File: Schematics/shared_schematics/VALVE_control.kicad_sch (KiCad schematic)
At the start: 7 parts, among them J2 SOL_CONN, Q1 AO3400A

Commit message: add requested changes for PR
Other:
- note added: "0.1 µF in 0603 for low parasitics and fast HF response; 10 µF in 1206 for larger bulk charge."
- note added: "package choice also affected by DC Bias Effect, higher cap MLCCs in smaller packages lose a significant pct of their effective capacitance."
- note added: "parallel decoupling circuit at the solenoid connector positive to suppress fast and slow transients and provide effective decoupling. 0.1 µF for high-frequency noise, 10 µF for bulk transient suppression."
- note added: "place caps together with flyback diode as close as possible to solenoid connector to minimize inductive voltage spikes and noise pickup"
- note added: "place the 0.1uF closer to the SOL input due to faster responsiveness (HF filter) the larger cap handles LF, therefore slightly less sensitive to placement"
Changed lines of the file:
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@@
+		)
+	)
+	(text "place the 0.1uF closer to the SOL input due to faster responsiveness (HF filter)\nthe larger cap handles LF, therefore slightly less sensitive to placement\n"
+		(exclude_from_sim no)
+		(at 86.868 81.026 0)
+		(effects
+			(font
+				(size 1.27 1.27)
+				(color 0 0 0 1)
+			)
+		)
+	)
+	(text "parallel decoupling circuit at the solenoid connector positive\nto suppress fast and slow transients and provide effective decoupling.\n\n0.1 µF for high-frequency noise, 10 µF for bulk transient suppression."
+		(exclude_from_sim no)
+		(at 88.138 116.332 0)
+		(effects
+			(font
+				(size 1.016 1.016)
+				(color 0 0 0 1)
+			)
+		)
+	)
+	(text "0.1 µF in 0603 for low parasitics and fast HF response; \n10 µF in 1206 for larger bulk charge."
+		(exclude_from_sim no)
+		(at 88.138 124.968 0)
+		(effects
+			(font
+				(size 1.016 1.016)
+				(color 0 0 0 1)
+			)
+		)
+	)
+	(text "place caps together with flyback diode as close as \npossible to solenoid connector to minimize inductive voltage spikes and noise pickup"
+		(exclude_from_sim no)
+		(at 87.376 74.422 0)
+		(effects
+			(font
+				(size 1.27 1.27)
+				(color 0 0 0 1)
+			)
+		)
+	)
+	(text "package choice also affected by DC Bias Effect, higher cap MLCCs \nin smaller packages lose a significant pct of their effective\ncapacitance."
+		(exclude_from_sim no)
+		(at 138.938 125.73 0)
+		(effects
+			(font
+				(size 1.016 1.016)
+				(color 0 0 0 1)
+			)
 		)
 	)
@@
 		(dnp no)
 		(fields_autoplaced yes)
-		(property "Reference" "#PWR0101"
+		(property "Reference" "#PWR0123"
 			(at 88.9 106.68 0)
 			(effects
@@
 		)
 	)
+	(sheet_instances
+		(path "/"
+			(page "1")
+		)
+	)

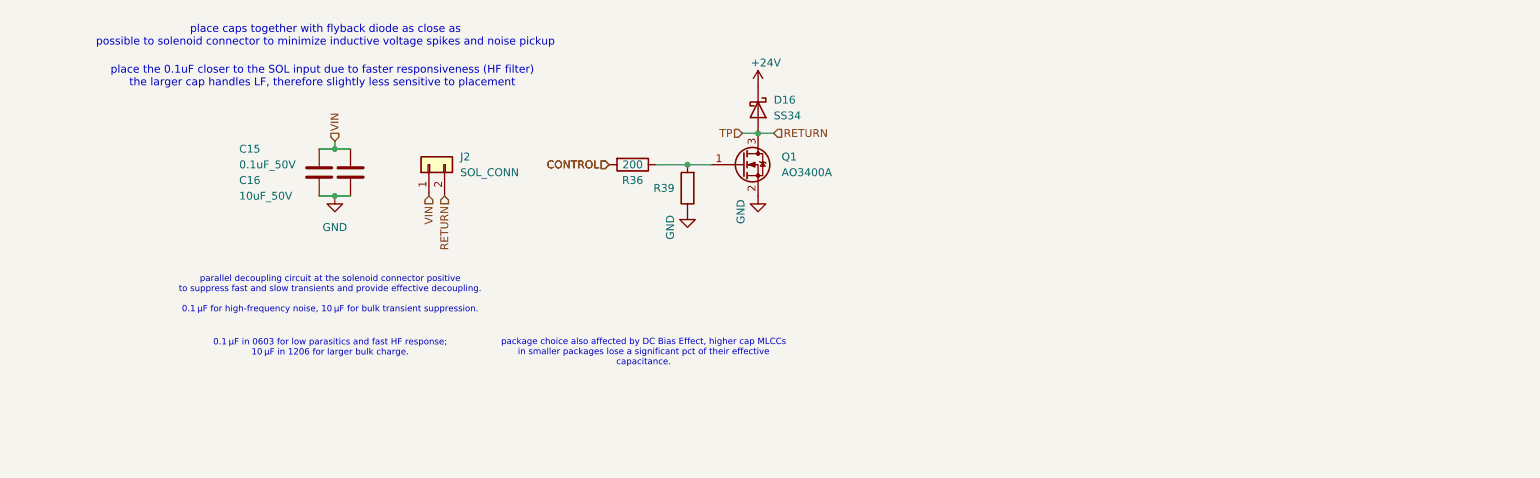
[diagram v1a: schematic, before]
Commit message: add all circuitry and missing datasheets
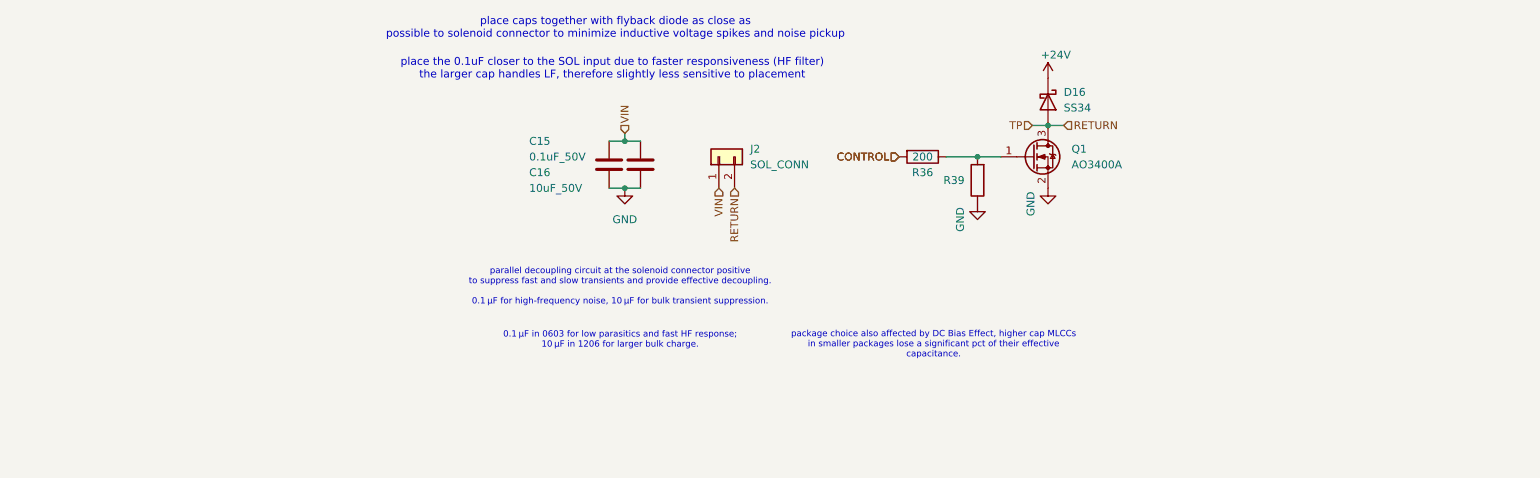
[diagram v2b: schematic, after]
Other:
- moved on the sheet: C15, C16, D16, J2, Q1, R36, R39

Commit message: pin assignments verified
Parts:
- J2: footprint CONNS:CONN02_530470260_MOL -> S02B_PASK_2:CONN2_S02B-PASK-2_JST
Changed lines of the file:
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@@
 			)
 		)
-		(property "Footprint" "CONNS:CONN02_530470260_MOL"
+		(property "Footprint" "S02B_PASK_2:CONN2_S02B-PASK-2_JST"
 			(at 151.13 93.98 0)
 			(effects

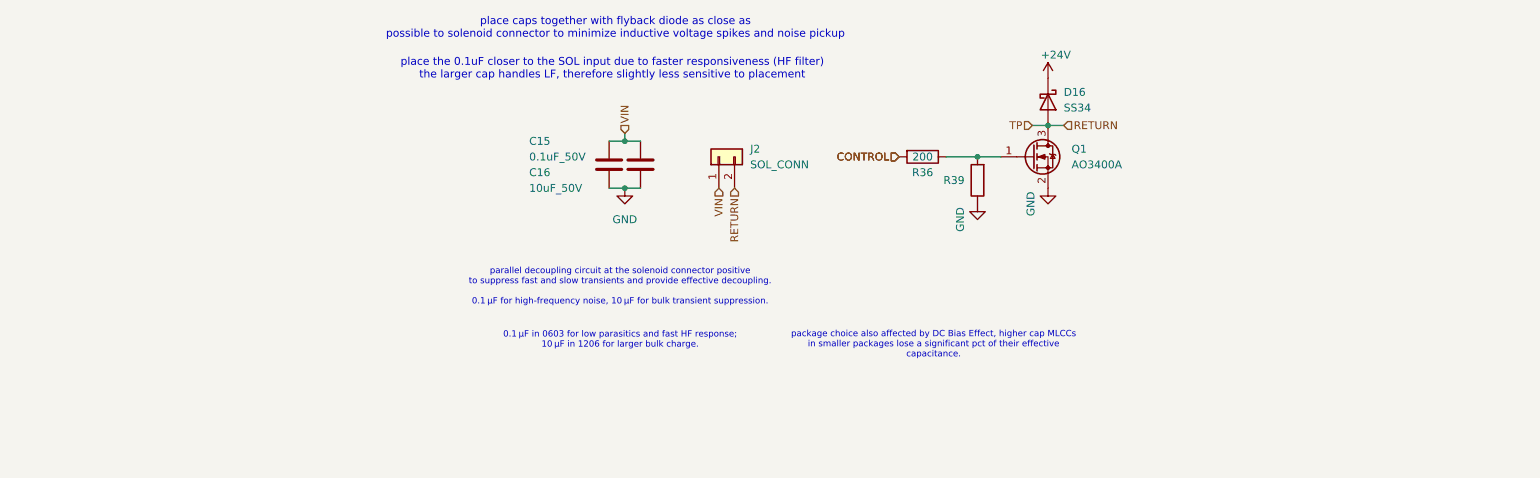
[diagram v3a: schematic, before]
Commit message: add power switching for PTs (schematic only)
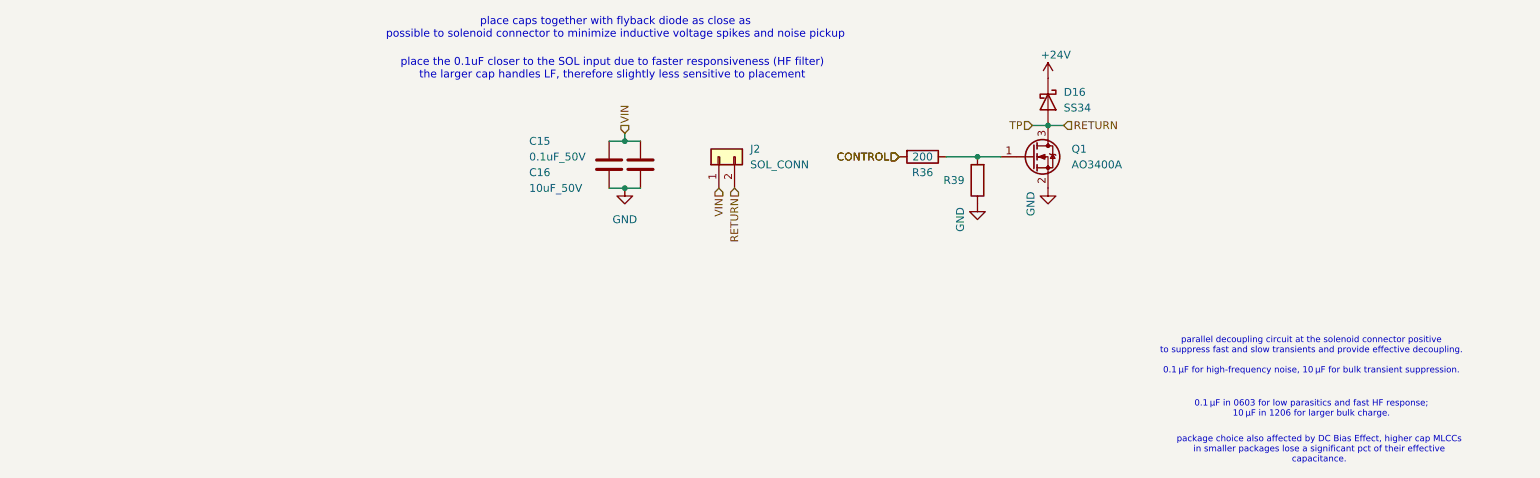
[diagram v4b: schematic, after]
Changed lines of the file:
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@@
 	(text "parallel decoupling circuit at the solenoid connector positive\nto suppress fast and slow transients and provide effective decoupling.\n\n0.1 µF for high-frequency noise, 10 µF for bulk transient suppression."
 		(exclude_from_sim no)
-		(at 135.128 115.062 0)
+		(at 247.142 126.238 0)
 		(effects
 			(font
@@
 	(text "0.1 µF in 0603 for low parasitics and fast HF response; \n10 µF in 1206 for larger bulk charge."
 		(exclude_from_sim no)
-		(at 135.128 123.698 0)
+		(at 247.142 134.874 0)
 		(effects
 			(font
@@
 	(text "package choice also affected by DC Bias Effect, higher cap MLCCs \nin smaller packages lose a significant pct of their effective\ncapacitance."
 		(exclude_from_sim no)
-		(at 185.928 124.46 0)
+		(at 248.412 141.478 0)
 		(effects
 			(font

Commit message: organizational work
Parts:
- C15: value 0.1uF_50V -> 0.1uF
- C16: value 10uF_50V -> 10uF
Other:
- note added: "place caps, FB-diode as close as possible to solenoid connectors."
- note removed: "0.1 µF in 0603 for low parasitics and fast HF response; 10 µF in 1206 for larger bulk charge."
- note removed: "package choice also affected by DC Bias Effect, higher cap MLCCs in smaller packages lose a significant pct of their effective capacitance."
- note removed: "parallel decoupling circuit at the solenoid connector positive to suppress fast and slow transients and provide effective decoupling. 0.1 µF for high-frequency noise, 10 µF for bulk transient suppression."
- note removed: "place caps together with flyback diode as close as possible to solenoid connector to minimize inductive voltage spikes and noise pickup"
- note removed: "place the 0.1uF closer to the SOL input due to faster responsiveness (HF filter) the larger cap handles LF, therefore slightly less sensitive to placement"
- moved on the sheet: C15, C16
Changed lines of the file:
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@@
 	)
 	(junction
-		(at 135.89 91.44)
+		(at 139.7 97.79)
 		(diameter 0)
 		(color 0 0 0 0)
@@
 	)
 	(junction
-		(at 135.89 99.06)
+		(at 139.7 90.17)
 		(diameter 0)
 		(color 0 0 0 0)
@@
 	(wire
 		(pts
-			(xy 135.89 90.17) (xy 135.89 91.44)
+			(xy 139.7 99.06) (xy 139.7 97.79)
 		)
 		(stroke
@@
 	(wire
 		(pts
-			(xy 135.89 91.44) (xy 138.43 91.44)
+			(xy 139.7 97.79) (xy 137.16 97.79)
 		)
 		(stroke
@@
 	(wire
 		(pts
-			(xy 133.35 99.06) (xy 135.89 99.06)
+			(xy 142.24 90.17) (xy 139.7 90.17)
 		)
 		(stroke
@@
 	(wire
 		(pts
-			(xy 133.35 91.44) (xy 135.89 91.44)
+			(xy 142.24 97.79) (xy 139.7 97.79)
 		)
 		(stroke
@@
 	(wire
 		(pts
-			(xy 135.89 99.06) (xy 138.43 99.06)
+			(xy 139.7 90.17) (xy 137.16 90.17)
 		)
 		(stroke
@@
 		)
 	)
-	(text "place the 0.1uF closer to the SOL input due to faster responsiveness (HF filter)\nthe larger cap handles LF, therefore slightly less sensitive to placement\n"
-		(exclude_from_sim no)
-		(at 133.858 79.756 0)
+	(text "place caps, FB-diode as close as possible \nto solenoid connectors."
+		(exclude_from_sim no)
+		(at 167.894 81.534 0)
 		(effects
 			(font
 				(size 1.27 1.27)
-				(color 0 0 0 1)
-			)
-		)
-	)
-	(text "parallel decoupling circuit at the solenoid connector positive\nto suppress fast and slow transients and provide effective decoupling.\n\n0.1 µF for high-frequency noise, 10 µF for bulk transient suppression."
-		(exclude_from_sim no)
-		(at 247.142 126.238 0)
-		(effects
-			(font
-				(size 1.016 1.016)
-				(color 0 0 0 1)
-			)
-		)
-	)
-	(text "0.1 µF in 0603 for low parasitics and fast HF response; \n10 µF in 1206 for larger bulk charge."
-		(exclude_from_sim no)
-		(at 247.142 134.874 0)
-		(effects
-			(font
-				(size 1.016 1.016)
-				(color 0 0 0 1)
-			)
-		)
-	)
-	(text "place caps together with flyback diode as close as \npossible to solenoid connector to minimize inductive voltage spikes and noise pickup"
-		(exclude_from_sim no)
-		(at 134.366 73.152 0)
-		(effects
-			(font
-				(size 1.27 1.27)
-				(color 0 0 0 1)
-			)
-		)
-	)
-	(text "package choice also affected by DC Bias Effect, higher cap MLCCs \nin smaller packages lose a significant pct of their effective\ncapacitance."
-		(exclude_from_sim no)
-		(at 248.412 141.478 0)
-		(effects
-			(font
-				(size 1.016 1.016)
 				(color 0 0 0 1)
 			)
@@
 	(hierarchical_label "VIN"
 		(shape input)
-		(at 135.89 90.17 90)
+		(at 139.7 99.06 270)
 		(fields_autoplaced yes)
 		(effects
@@
 				(size 1.27 1.27)
 			)
-			(justify left)
+			(justify right)
 		)
 	)
@@
 				)
 			)
-			(project "upper_lc_board"
-				(path "/d63798c4-e363-437e-9012-e4aff32e6642/762489dd-fdf2-4f5c-8c0c-d0a6195d3f58/294431a1-b811-4a1d-b2a9-ae58ba2678b8"
-					(reference "Q1")
-					(unit 1)
-				)
-				(path "/d63798c4-e363-437e-9012-e4aff32e6642/762489dd-fdf2-4f5c-8c0c-d0a6195d3f58/ba318d50-d24b-43da-9443-1d352fb2a38b"
-					(reference "Q2")
-					(unit 1)
-				)
-			)
 		)
 	)
@@
 				)
 			)
-			(project "upper_lc_board"
-				(path "/d63798c4-e363-437e-9012-e4aff32e6642/762489dd-fdf2-4f5c-8c0c-d0a6195d3f58/294431a1-b811-4a1d-b2a9-ae58ba2678b8"
-					(reference "D16")
-					(unit 1)
-				)
-				(path "/d63798c4-e363-437e-9012-e4aff32e6642/762489dd-fdf2-4f5c-8c0c-d0a6195d3f58/ba318d50-d24b-43da-9443-1d352fb2a38b"
-					(reference "D15")
-					(unit 1)
-				)
-			)
 		)
 	)
 	(symbol
 		(lib_id "power:GND")
-		(at 135.89 99.06 0)
+		(at 139.7 90.17 180)
 		(unit 1)
 		(exclude_from_sim no)
@@
 		(fields_autoplaced yes)
 		(property "Reference" "#PWR0123"
-			(at 135.89 105.41 0)
+			(at 139.7 83.82 0)
 			(effects
 				(font
@@
 		)
 		(property "Value" "GND"
-			(at 135.89 104.14 0)
+			(at 139.7 85.09 0)
 			(effects
 				(font
@@
 		)
 		(property "Footprint" ""
-			(at 135.89 99.06 0)
+			(at 139.7 90.17 0)
 			(effects
 				(font
@@
 		)
 		(property "Datasheet" ""
-			(at 135.89 99.06 0)
+			(at 139.7 90.17 0)
 			(effects
 				(font
@@
 		)
 		(property "Description" "Power symbol creates a global label with name \"GND\" , ground"
-			(at 135.89 99.06 0)
+			(at 139.7 90.17 0)
 			(effects
 				(font
@@
 	(symbol
 		(lib_id "Device:C")
-		(at 138.43 95.25 0)
+		(at 137.16 93.98 180)
 		(unit 1)
 		(exclude_from_sim no)
@@
 		(dnp no)
 		(property "Reference" "C16"
-			(at 120.396 96.52 0)
+			(at 132.08 90.17 0)
 			(effects
 				(font
@@
 			)
 		)
-		(property "Value" "10uF_50V"
-			(at 120.396 99.06 0)
+		(property "Value" "10uF"
+			(at 132.08 92.71 0)
 			(effects
 				(font
@@
 		)
 		(property "Footprint" "Capacitor_SMD:C_1206_3216Metric"
-			(at 139.3952 99.06 0)
+			(at 136.1948 90.17 0)
 			(effects
 				(font
@@
 		)
 		(property "Datasheet" "~"
-			(at 138.43 95.25 0)
+			(at 137.16 93.98 0)
 			(effects
 				(font
@@
 		)
 		(property "Description" "Unpolarized capacitor"
-			(at 138.43 95.25 0)
+			(at 137.16 93.98 0)
 			(effects
 				(font
@@
 				)
 			)
-			(project "upper_lc_board"
-				(path "/d63798c4-e363-437e-9012-e4aff32e6642/762489dd-fdf2-4f5c-8c0c-d0a6195d3f58/294431a1-b811-4a1d-b2a9-ae58ba2678b8"
-					(reference "R42")
-					(unit 1)
-				)
-				(path "/d63798c4-e363-437e-9012-e4aff32e6642/762489dd-fdf2-4f5c-8c0c-d0a6195d3f58/ba318d50-d24b-43da-9443-1d352fb2a38b"
-					(reference "R39")
-					(unit 1)
-				)
-			)
 		)
 	)
@@
 				)
 			)
-			(project "upper_lc_board"
-				(path "/d63798c4-e363-437e-9012-e4aff32e6642/762489dd-fdf2-4f5c-8c0c-d0a6195d3f58/294431a1-b811-4a1d-b2a9-ae58ba2678b8"
-					(reference "R41")
-					(unit 1)
-				)
-				(path "/d63798c4-e363-437e-9012-e4aff32e6642/762489dd-fdf2-4f5c-8c0c-d0a6195d3f58/ba318d50-d24b-43da-9443-1d352fb2a38b"
-					(reference "R36")
-					(unit 1)
-				)
-			)
 		)
 	)
@@
 				)
 			)
-			(project "upper_lc_board"
-				(path "/d63798c4-e363-437e-9012-e4aff32e6642/762489dd-fdf2-4f5c-8c0c-d0a6195d3f58/294431a1-b811-4a1d-b2a9-ae58ba2678b8"
-					(reference "#PWR0125")
-					(unit 1)
-				)
-				(path "/d63798c4-e363-437e-9012-e4aff32e6642/762489dd-fdf2-4f5c-8c0c-d0a6195d3f58/ba318d50-d24b-43da-9443-1d352fb2a38b"
-					(reference "#PWR0104")
-					(unit 1)
-				)
-			)
 		)
 	)
@@
 	(symbol
 		(lib_id "Device:C")
-		(at 133.35 95.25 0)
+		(at 142.24 93.98 180)
 		(unit 1)
 		(exclude_from_sim no)
@@
 		(dnp no)
 		(property "Reference" "C15"
-			(at 120.396 91.44 0)
+			(at 132.334 94.996 0)
 			(effects
 				(font
@@
 			)
 		)
-		(property "Value" "0.1uF_50V"
-			(at 120.396 93.98 0)
+		(property "Value" "0.1uF"
+			(at 132.334 97.536 0)
 			(effects
 				(font
@@
 		)
 		(property "Footprint" "Capacitor_SMD:C_0603_1608Metric"
-			(at 134.3152 99.06 0)
+			(at 141.2748 90.17 0)
 			(effects
 				(font
@@
 		)
 		(property "Datasheet" "~"
-			(at 133.35 95.25 0)
+			(at 142.24 93.98 0)
 			(effects
 				(font
@@
 		)
 		(property "Description" "Unpolarized capacitor"
-			(at 133.35 95.25 0)
+			(at 142.24 93.98 0)
 			(effects
 				(font
@@
 				)
 			)
-			(project "upper_lc_board"
-				(path "/d63798c4-e363-437e-9012-e4aff32e6642/762489dd-fdf2-4f5c-8c0c-d0a6195d3f58/294431a1-b811-4a1d-b2a9-ae58ba2678b8"
-					(reference "#PWR0124")
-					(unit 1)
-				)
-				(path "/d63798c4-e363-437e-9012-e4aff32e6642/762489dd-fdf2-4f5c-8c0c-d0a6195d3f58/ba318d50-d24b-43da-9443-1d352fb2a38b"
-					(reference "#PWR0105")
-					(unit 1)
-				)
-			)
 		)
 	)
@@
 					(unit 1)
 				)
-			)
-			(project "upper_lc_board"
-				(path "/d63798c4-e363-437e-9012-e4aff32e6642/762489dd-fdf2-4f5c-8c0c-d0a6195d3f58/294431a1-b811-4a1d-b2a9-ae58ba2678b8"
-					(reference "#PWR0103")
-					(unit 1)
-				)
-				(path "/d63798c4-e363-437e-9012-e4aff32e6642/762489dd-fdf2-4f5c-8c0c-d0a6195d3f58/ba318d50-d24b-43da-9443-1d352fb2a38b"
-					(reference "#PWR0107")
-					(unit 1)
-				)

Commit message: more organizational work, add shared footprint, model, symbol dirs and clean up individuals
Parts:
- J2: footprint S02B_PASK_2:CONN2_S02B-PASK-2_JST -> ul_B02B-PASK-1:CONN_B02B-PASK-1_JST
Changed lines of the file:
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@@
 			)
 		)
-		(property "Datasheet" "${KIPRJMOD}/../../Datasheets/MOSFET-AO3400A.pdf"
+		(property "Datasheet" "${KIPRJMOD}/../../Documentation/mosfet_AO3400A_DS.pdf"
 			(at 207.01 97.79 0)
 			(effects
@@
 				)
 				(path "/9b1a1d2a-fad7-4f10-83f3-1f83e9656c75/f003a3ad-0ca0-4253-bb6a-1aee93b0e37f/65115d6c-240a-4886-8e54-c37424bab0b6"
+					(reference "Q2")
+					(unit 1)
+				)
+			)
+			(project ""
+				(path "/d63798c4-e363-437e-9012-e4aff32e6642/762489dd-fdf2-4f5c-8c0c-d0a6195d3f58/294431a1-b811-4a1d-b2a9-ae58ba2678b8"
+					(reference "Q1")
+					(unit 1)
+				)
+				(path "/d63798c4-e363-437e-9012-e4aff32e6642/762489dd-fdf2-4f5c-8c0c-d0a6195d3f58/ba318d50-d24b-43da-9443-1d352fb2a38b"
 					(reference "Q2")
 					(unit 1)
@@
 			)
 		)
-		(property "Datasheet" "https://www.vishay.com/docs/88751/ss32.pdf"
+		(property "Datasheet" "${KIPRJMOD}/../../Documentation/schottky_diode_SS39-D_DS.pdf"
 			(at 204.47 85.09 0)
 			(effects
@@
 				(path "/9b1a1d2a-fad7-4f10-83f3-1f83e9656c75/f003a3ad-0ca0-4253-bb6a-1aee93b0e37f/65115d6c-240a-4886-8e54-c37424bab0b6"
 					(reference "D17")
+					(unit 1)
+				)
+			)
+			(project ""
+				(path "/d63798c4-e363-437e-9012-e4aff32e6642/762489dd-fdf2-4f5c-8c0c-d0a6195d3f58/294431a1-b811-4a1d-b2a9-ae58ba2678b8"
+					(reference "D16")
+					(unit 1)
+				)
+				(path "/d63798c4-e363-437e-9012-e4aff32e6642/762489dd-fdf2-4f5c-8c0c-d0a6195d3f58/ba318d50-d24b-43da-9443-1d352fb2a38b"
+					(reference "D15")
 					(unit 1)
 				)
@@
 				)
 			)
+			(project ""
+				(path "/d63798c4-e363-437e-9012-e4aff32e6642/762489dd-fdf2-4f5c-8c0c-d0a6195d3f58/294431a1-b811-4a1d-b2a9-ae58ba2678b8"
+					(reference "R39")
+					(unit 1)
+				)
+				(path "/d63798c4-e363-437e-9012-e4aff32e6642/762489dd-fdf2-4f5c-8c0c-d0a6195d3f58/ba318d50-d24b-43da-9443-1d352fb2a38b"
+					(reference "R42")
+					(unit 1)
+				)
+			)
 		)
 	)
@@
 				)
 			)
+			(project ""
+				(path "/d63798c4-e363-437e-9012-e4aff32e6642/762489dd-fdf2-4f5c-8c0c-d0a6195d3f58/294431a1-b811-4a1d-b2a9-ae58ba2678b8"
+					(reference "R36")
+					(unit 1)
+				)
+				(path "/d63798c4-e363-437e-9012-e4aff32e6642/762489dd-fdf2-4f5c-8c0c-d0a6195d3f58/ba318d50-d24b-43da-9443-1d352fb2a38b"
+					(reference "R41")
+					(unit 1)
+				)
+			)
 		)
 	)
@@
 				)
 			)
+			(project ""
+				(path "/d63798c4-e363-437e-9012-e4aff32e6642/762489dd-fdf2-4f5c-8c0c-d0a6195d3f58/294431a1-b811-4a1d-b2a9-ae58ba2678b8"
+					(reference "#PWR0125")
+					(unit 1)
+				)
+				(path "/d63798c4-e363-437e-9012-e4aff32e6642/762489dd-fdf2-4f5c-8c0c-d0a6195d3f58/ba318d50-d24b-43da-9443-1d352fb2a38b"
+					(reference "#PWR0105")
+					(unit 1)
+				)
+			)
 		)
 	)
@@
 			)
 		)
-		(property "Footprint" "S02B_PASK_2:CONN2_S02B-PASK-2_JST"
+		(property "Footprint" "ul_B02B-PASK-1:CONN_B02B-PASK-1_JST"
 			(at 151.13 93.98 0)
 			(effects
@@
 			)
 		)
-		(property "Datasheet" "${KIPRJMOD}/../../Datasheets/CONN-530470460.pdf"
+		(property "Datasheet" "${KIPRJMOD}/../../Documentation/conn_jst_B0XB-PASK-1_DS.pdf"
 			(at 151.13 93.98 0)
 			(effects
@@
 				)
 			)
+			(project ""
+				(path "/d63798c4-e363-437e-9012-e4aff32e6642/762489dd-fdf2-4f5c-8c0c-d0a6195d3f58/294431a1-b811-4a1d-b2a9-ae58ba2678b8"
+					(reference "#PWR0124")
+					(unit 1)
+				)
+				(path "/d63798c4-e363-437e-9012-e4aff32e6642/762489dd-fdf2-4f5c-8c0c-d0a6195d3f58/ba318d50-d24b-43da-9443-1d352fb2a38b"
+					(reference "#PWR0104")
+					(unit 1)
+				)
+			)
 		)
 	)
@@
 					(unit 1)
 				)
+			)
+			(project ""
+				(path "/d63798c4-e363-437e-9012-e4aff32e6642/762489dd-fdf2-4f5c-8c0c-d0a6195d3f58/294431a1-b811-4a1d-b2a9-ae58ba2678b8"
+					(reference "#PWR0103")
+					(unit 1)
+				)
+				(path "/d63798c4-e363-437e-9012-e4aff32e6642/762489dd-fdf2-4f5c-8c0c-d0a6195d3f58/ba318d50-d24b-43da-9443-1d352fb2a38b"
+					(reference "#PWR0107")
+					(unit 1)
+				)

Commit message: routing work
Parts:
- C15: JLCPCB (none) -> C14663
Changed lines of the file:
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@@
+			)
+		)
+		(property "JLCPCB" "C14663"
+			(at 142.24 93.98 0)
+			(effects
+				(font
+					(size 1.27 1.27)
+				)
+				(hide yes)
 			)
 		)
